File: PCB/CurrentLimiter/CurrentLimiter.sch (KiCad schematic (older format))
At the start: 22 parts, among them P1 CONN_01X06, Q1 Q_PMOS_DGS, Q2 2N2222, Q3 2N2222, Q4 2N2222, U1 LM358

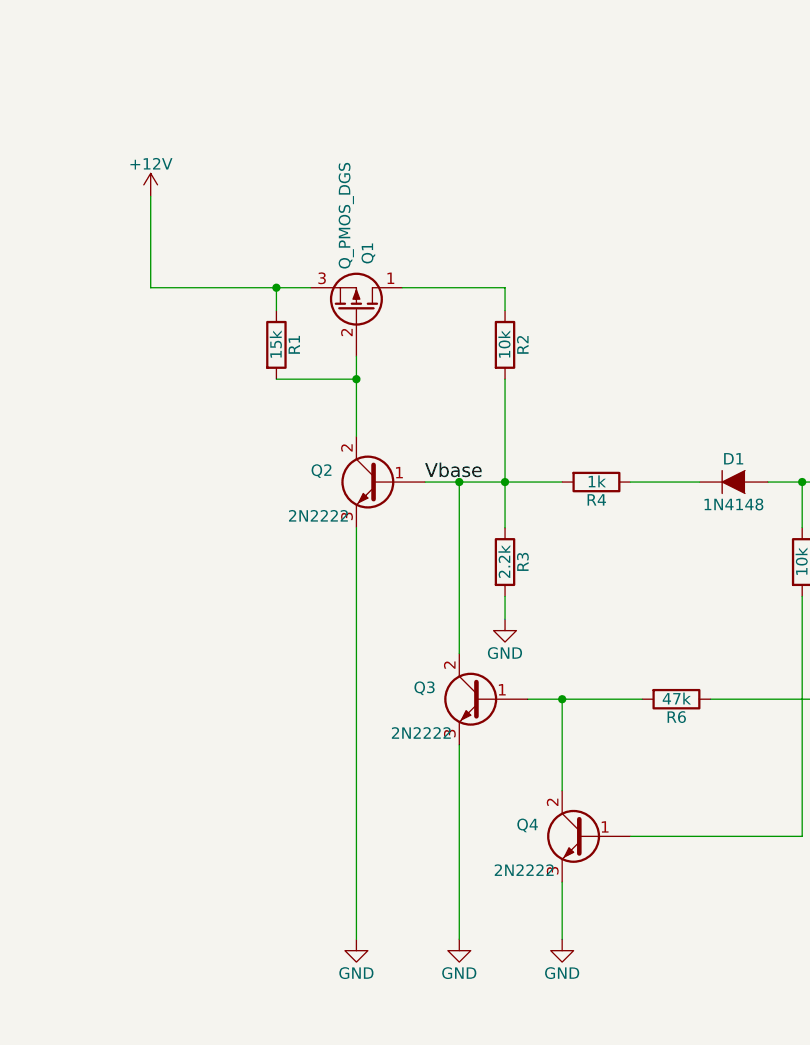
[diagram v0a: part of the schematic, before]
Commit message: Footprints for transistors added
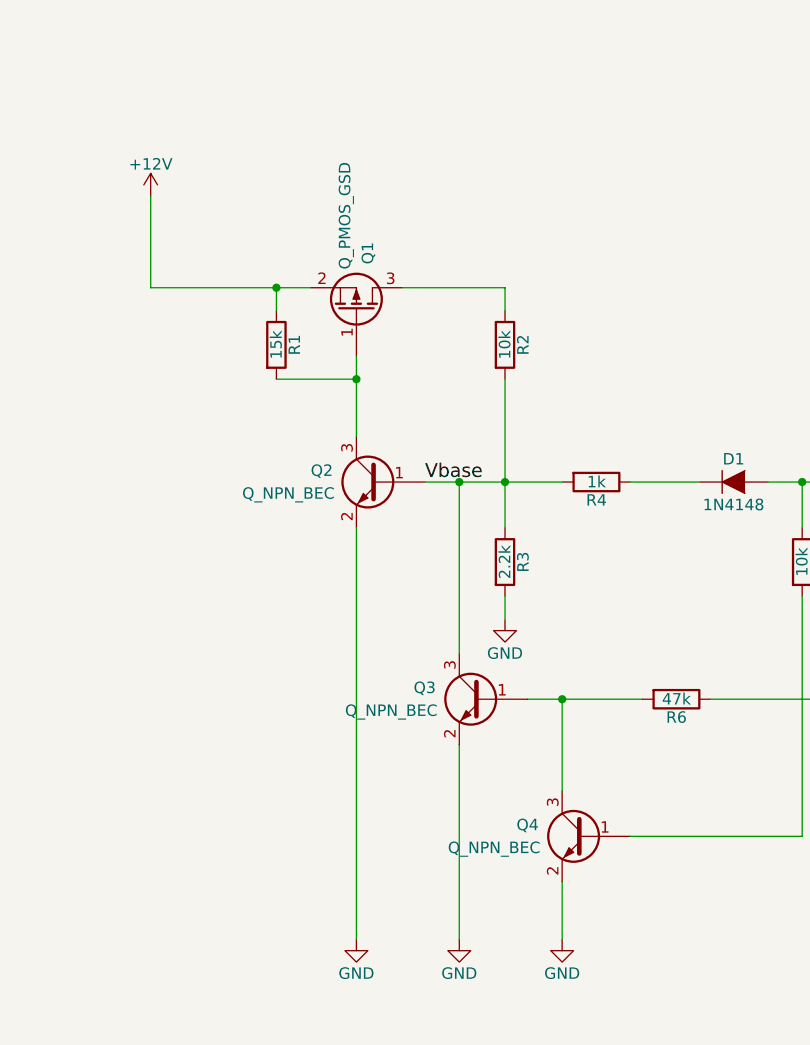
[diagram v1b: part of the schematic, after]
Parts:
- removed Q1: Q_PMOS_DGS, symbol Q_PMOS_DGS
- removed Q2, Q3, Q4: 2N2222, TO_SOT_Packages_SMD:SOT-23_Handsoldering, symbol Q_NPN_BCE
- added Q1: Q_PMOS_GSD, TO_SOT_Packages_SMD:SOT-23_Handsoldering, symbol Q_PMOS_GSD
- added Q2, Q3, Q4: Q_NPN_BEC, TO_SOT_Packages_SMD:SOT-23_Handsoldering, symbol Q_NPN_BEC
- D1: footprint (none) -> Diodes_SMD:D_SOD-123
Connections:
- net +12V: now also Q1.2 (S)
- net GND: now also Q2.2 (E), Q3.2 (E), Q4.2 (E)
- net Vbase: now also Q2.1 (B), Q3.3 (C)
- net at R2.1: now also Q1.3 (D)
- net at R1.2: now also Q1.1 (G), Q2.3 (C)
- net at R6.2: now also Q3.1 (B), Q4.3 (C)
- net at R5.2: now also Q4.1 (B)
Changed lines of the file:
@@
 LIBS:contrib
 LIBS:valves
+LIBS:CurrentLimiter-cache
 EELAYER 25 0
 EELAYER END
@@
 $EndDescr
 $Comp
-L Q_PMOS_DGS Q1
-U 1 1 58E136A7
-P 3450 2550
-F 0 "Q1" H 3750 2600 50  0000 R CNN
-F 1 "Q_PMOS_DGS" H 4100 2500 50  0000 R CNN
-F 2 "" H 3650 2650 50  0001 C CNN
-F 3 "" H 3450 2550 50  0000 C CNN
-	1    3450 2550
-	0    1    -1   0
-$EndComp
-$Comp
-L Q_NPN_BCE Q2
-U 1 1 58E1386B
-P 3550 3300
-F 0 "Q2" H 3850 3350 50  0000 R CNN
-F 1 "2N2222" H 3950 3150 50  0000 R CNN
-F 2 "TO_SOT_Packages_SMD:SOT-23_Handsoldering" H 3750 3400 50  0001 C CNN
-F 3 "" H 3550 3300 50  0000 C CNN
-	1    3550 3300
-	-1   0    0    -1
-$EndComp
-$Comp
 L R R1
 U 1 1 58E138AA
@@
 Connection ~ 3450 2850
 $Comp
-L Q_NPN_BCE Q3
-U 1 1 58E13A50
-P 4000 4250
-F 0 "Q3" H 4300 4300 50  0000 R CNN
-F 1 "2N2222" H 4400 4100 50  0000 R CNN
-F 2 "TO_SOT_Packages_SMD:SOT-23_Handsoldering" H 4200 4350 50  0001 C CNN
-F 3 "" H 4000 4250 50  0000 C CNN
-	1    4000 4250
-	-1   0    0    -1
-$EndComp
-$Comp
-L Q_NPN_BCE Q4
-U 1 1 58E13A9F
-P 4450 4850
-F 0 "Q4" H 4750 4900 50  0000 R CNN
-F 1 "2N2222" H 4850 4700 50  0000 R CNN
-F 2 "TO_SOT_Packages_SMD:SOT-23_Handsoldering" H 4650 4950 50  0001 C CNN
-F 3 "" H 4450 4850 50  0000 C CNN
-	1    4450 4850
-	-1   0    0    -1
-$EndComp
-$Comp
 L R R2
 U 1 1 58E13BAC
@@
 F 0 "D1" H 5100 3400 50  0000 C CNN
 F 1 "1N4148" H 5100 3200 50  0000 C CNN
-F 2 "" H 5100 3300 50  0001 C CNN
+F 2 "Diodes_SMD:D_SOD-123" H 5100 3300 50  0001 C CNN
 F 3 "" H 5100 3300 50  0000 C CNN
 	1    5100 3300
@@
 Connection ~ 3100 2450
 $Comp
-L GND #PWR01
+L GND #PWR5
 U 1 1 58E14C1E
 P 4350 5300
-F 0 "#PWR01" H 4350 5050 50  0001 C CNN
+F 0 "#PWR5" H 4350 5050 50  0001 C CNN
 F 1 "GND" H 4350 5150 50  0000 C CNN
 F 2 "" H 4350 5300 50  0000 C CNN
@@
 $EndComp
 $Comp
-L GND #PWR02
+L GND #PWR3
 U 1 1 58E14C51
 P 3900 5300
-F 0 "#PWR02" H 3900 5050 50  0001 C CNN
+F 0 "#PWR3" H 3900 5050 50  0001 C CNN
 F 1 "GND" H 3900 5150 50  0000 C CNN
 F 2 "" H 3900 5300 50  0000 C CNN
@@
 	3900 5300 3900 4450
 $Comp
-L GND #PWR03
+L GND #PWR2
 U 1 1 58E14DA9
 P 3450 5300
-F 0 "#PWR03" H 3450 5050 50  0001 C CNN
+F 0 "#PWR2" H 3450 5050 50  0001 C CNN
 F 1 "GND" H 3450 5150 50  0000 C CNN
 F 2 "" H 3450 5300 50  0000 C CNN
@@
 	3450 5300 3450 3500
 $Comp
-L GND #PWR04
+L GND #PWR4
 U 1 1 58E14FAF
 P 4100 3900
-F 0 "#PWR04" H 4100 3650 50  0001 C CNN
+F 0 "#PWR4" H 4100 3650 50  0001 C CNN
 F 1 "GND" H 4100 3750 50  0000 C CNN
 F 2 "" H 4100 3900 50  0000 C CNN
@@
 	5000 4250 6050 4250
 $Comp
-L GND #PWR05
+L GND #PWR7
 U 1 1 58E15CDD
 P 6450 5300
-F 0 "#PWR05" H 6450 5050 50  0001 C CNN
+F 0 "#PWR7" H 6450 5050 50  0001 C CNN
 F 1 "GND" H 6450 5150 50  0000 C CNN
 F 2 "" H 6450 5300 50  0000 C CNN
@@
 Connection ~ 8400 4450
 $Comp
-L GND #PWR06
+L GND #PWR10
 U 1 1 58E17521
 P 8400 5300
-F 0 "#PWR06" H 8400 5050 50  0001 C CNN
+F 0 "#PWR10" H 8400 5050 50  0001 C CNN
 F 1 "GND" H 8400 5150 50  0000 C CNN
 F 2 "" H 8400 5300 50  0000 C CNN
@@
 	8400 5300 8400 5000
 $Comp
-L GND #PWR07
+L GND #PWR9
 U 1 1 58E17943
 P 8050 5300
-F 0 "#PWR07" H 8050 5050 50  0001 C CNN
+F 0 "#PWR9" H 8050 5050 50  0001 C CNN
 F 1 "GND" H 8050 5150 50  0000 C CNN
 F 2 "" H 8050 5300 50  0000 C CNN
@@
 	6850 4150 6850 3300
 $Comp
-L +12V #PWR08
+L +12V #PWR1
 U 1 1 58E198F4
 P 2550 2050
-F 0 "#PWR08" H 2550 1900 50  0001 C CNN
+F 0 "#PWR1" H 2550 1900 50  0001 C CNN
 F 1 "+12V" H 2550 2190 50  0000 C CNN
 F 2 "" H 2550 2050 50  0000 C CNN
@@
 	2550 2450 2550 2050
 $Comp
-L +12V #PWR09
+L +12V #PWR6
 U 1 1 58E1998A
 P 6450 3650
-F 0 "#PWR09" H 6450 3500 50  0001 C CNN
+F 0 "#PWR6" H 6450 3500 50  0001 C CNN
 F 1 "+12V" H 6450 3790 50  0000 C CNN
 F 2 "" H 6450 3650 50  0000 C CNN
@@
 	6450 3950 6450 3650
 $Comp
-L +12V #PWR010
+L +12V #PWR8
 U 1 1 58E19BCF
 P 8050 3650
-F 0 "#PWR010" H 8050 3500 50  0001 C CNN
+F 0 "#PWR8" H 8050 3500 50  0001 C CNN
 F 1 "+12V" H 8050 3790 50  0000 C CNN
 F 2 "" H 8050 3650 50  0000 C CNN
@@
 $EndComp
 $Comp
-L +12V #PWR011
+L +12V #PWR11
 U 1 1 58E1E64F
 P 8950 900
-F 0 "#PWR011" H 8950 750 50  0001 C CNN
+F 0 "#PWR11" H 8950 750 50  0001 C CNN
 F 1 "+12V" H 8950 1040 50  0000 C CNN
 F 2 "" H 8950 900 50  0000 C CNN
@@
 $EndComp
 $Comp
-L GND #PWR012
+L GND #PWR12
 U 1 1 58E1E812
 P 9000 1800
-F 0 "#PWR012" H 9000 1550 50  0001 C CNN
+F 0 "#PWR12" H 9000 1550 50  0001 C CNN
 F 1 "GND" H 9000 1650 50  0000 C CNN
 F 2 "" H 9000 1800 50  0000 C CNN
@@
 Wire Wire Line
 	2550 2450 3250 2450
+$Comp
+L Q_NPN_BEC Q2
+U 1 1 58E4ED74
+P 3550 3300
+F 0 "Q2" H 3850 3350 50  0000 R CNN
+F 1 "Q_NPN_BEC" H 4150 3250 50  0000 R CNN
+F 2 "TO_SOT_Packages_SMD:SOT-23_Handsoldering" H 3750 3400 50  0001 C CNN
+F 3 "http://lv.farnell.com/nxp/bcx70h/transistor-npn-sot-23/dp/1081282" H 3550 3300 50  0001 C CNN
+F 4 "http://lv.farnell.com/fairchild-semiconductor/bcw66g/transistor-npn-smd-sot-23/dp/1467891" H 3550 3300 60  0001 C CNN "Alternate part"
+	1    3550 3300
+	-1   0    0    -1
+$EndComp
+$Comp
+L Q_NPN_BEC Q3
+U 1 1 58E4F17E
+P 4000 4250
+F 0 "Q3" H 4300 4300 50  0000 R CNN
+F 1 "Q_NPN_BEC" H 4600 4200 50  0000 R CNN
+F 2 "TO_SOT_Packages_SMD:SOT-23_Handsoldering" H 4200 4350 50  0001 C CNN
+F 3 "http://lv.farnell.com/nxp/bcx70h/transistor-npn-sot-23/dp/1081282" H 4000 4250 50  0001 C CNN
+F 4 "http://lv.farnell.com/fairchild-semiconductor/bcw66g/transistor-npn-smd-sot-23/dp/1467891" H 4000 4250 60  0001 C CNN "Alternate part"
+	1    4000 4250
+	-1   0    0    -1
+$EndComp
+$Comp
+L Q_NPN_BEC Q4
+U 1 1 58E4F224
+P 4450 4850
+F 0 "Q4" H 4750 4900 50  0000 R CNN
+F 1 "Q_NPN_BEC" H 5050 4800 50  0000 R CNN
+F 2 "TO_SOT_Packages_SMD:SOT-23_Handsoldering" H 4650 4950 50  0001 C CNN
+F 3 "http://lv.farnell.com/nxp/bcx70h/transistor-npn-sot-23/dp/1081282" H 4450 4850 50  0001 C CNN
+F 4 "http://lv.farnell.com/fairchild-semiconductor/bcw66g/transistor-npn-smd-sot-23/dp/1467891" H 4450 4850 60  0001 C CNN "Alternate part"
+	1    4450 4850
+	-1   0    0    -1
+$EndComp
+$Comp
+L Q_PMOS_GSD Q1
+U 1 1 58E4F551
+P 3450 2550
+F 0 "Q1" H 3750 2600 50  0000 R CNN
+F 1 "Q_PMOS_GSD" H 4100 2500 50  0000 R CNN
+F 2 "TO_SOT_Packages_SMD:SOT-23_Handsoldering" H 3650 2650 50  0001 C CNN
+F 3 "http://lv.farnell.com/infineon/irlml9301trpbf/mosfet-diode-p-ch-30v-3-6a-sot23/dp/1831089" H 3450 2550 50  0001 C CNN
+	1    3450 2550
+	0    1    -1   0
+$EndComp
 $EndSCHEMATC

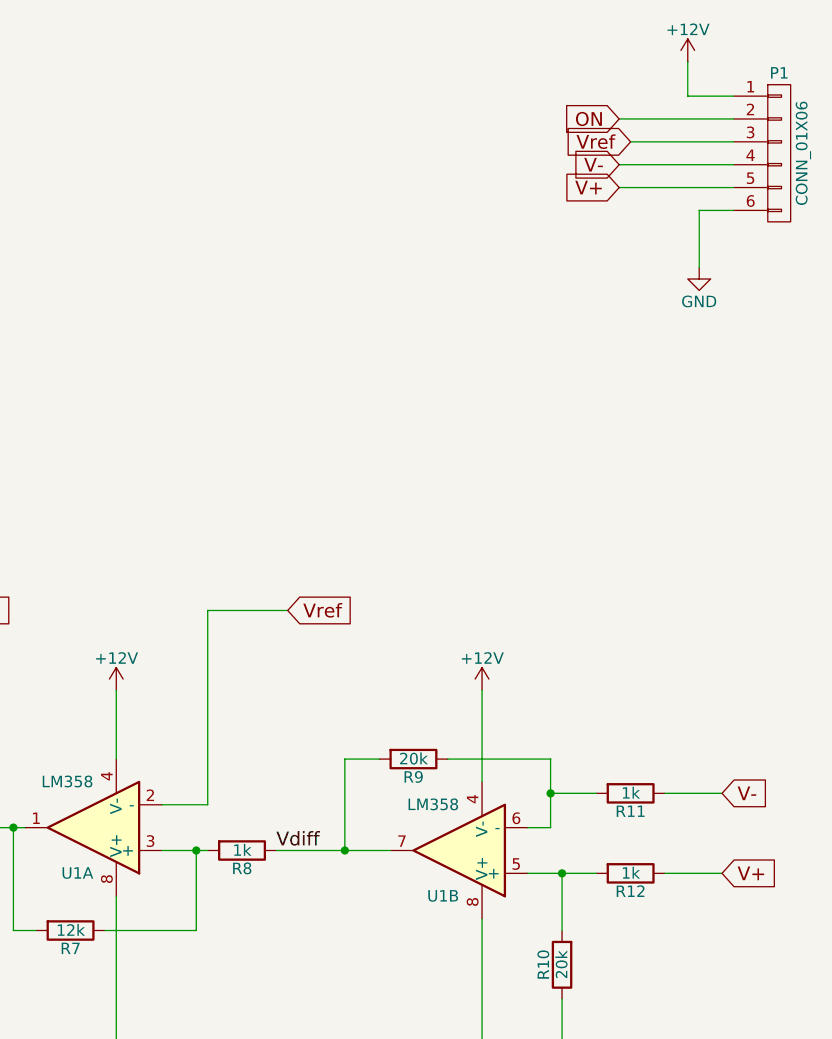
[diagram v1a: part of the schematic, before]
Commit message: Added header connectors for OpAmp modules
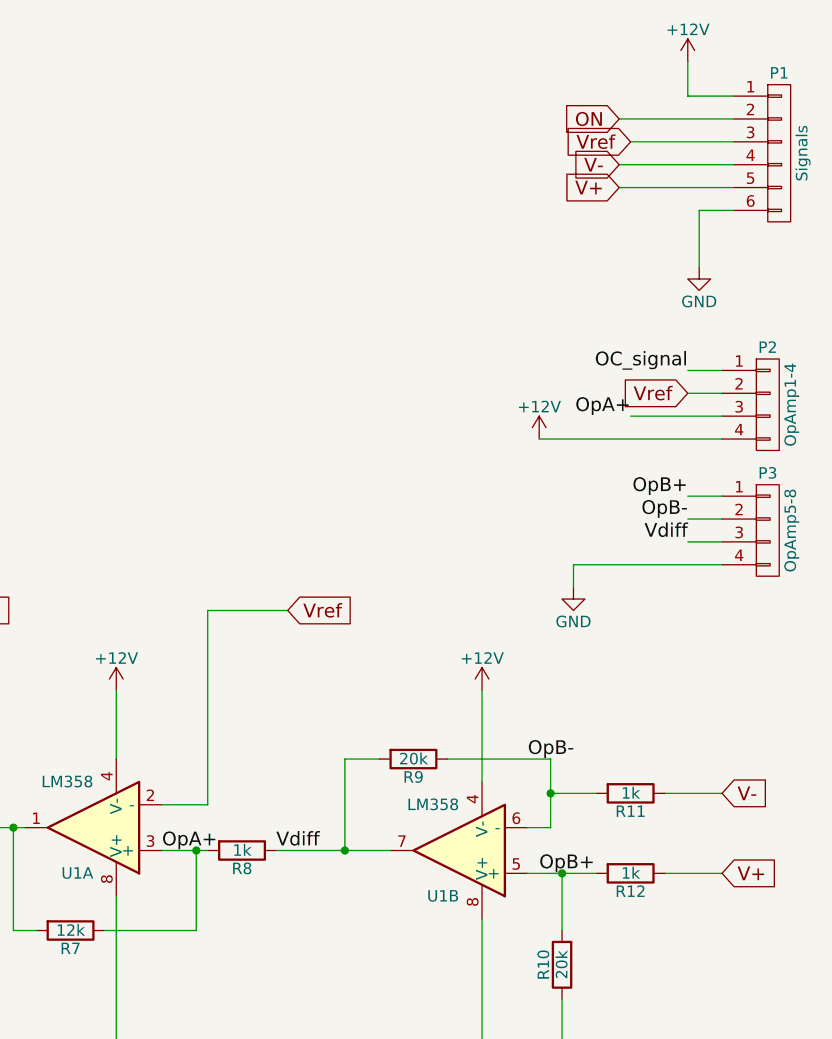
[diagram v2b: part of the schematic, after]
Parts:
- added P2: OpAmp1-4, symbol CONN_01X04
- added P3: OpAmp5-8, symbol CONN_01X04
- P1: value CONN_01X06 -> Signals
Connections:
- net +12V: now also P2.4 (P4)
- net GND: now also P3.4 (P4)
- net OC_signal: now also P2.1 (P1)
- net Vdiff: now also P3.3 (P3)
- net Vref: now also P2.2 (P2)
- net OpA+: now reaches R7.1, R8.2, U1.3 (+)
- net OpA+: now also P2.3 (P3)
- net OpB+: now reaches R10.2, R12.2, U1.5 (+)
- net OpB+: now also P3.1 (P1)
- net OpB-: now reaches R11.2, R9.1, U1.6 (-)
- net OpB-: now also P3.2 (P2)
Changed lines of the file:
@@
 Connection ~ 8400 4450
 $Comp
-L GND #PWR10
+L GND #PWR11
 U 1 1 58E17521
 P 8400 5300
-F 0 "#PWR10" H 8400 5050 50  0001 C CNN
+F 0 "#PWR11" H 8400 5050 50  0001 C CNN
 F 1 "GND" H 8400 5150 50  0000 C CNN
 F 2 "" H 8400 5300 50  0000 C CNN
@@
 P 9350 1300
 F 0 "P1" H 9350 1650 50  0000 C CNN
-F 1 "CONN_01X06" V 9450 1300 50  0000 C CNN
+F 1 "Signals" V 9450 1300 50  0000 C CNN
 F 2 "Pin_Headers:Pin_Header_Straight_1x06_Pitch2.54mm" H 9350 1300 50  0001 C CNN
 F 3 "" H 9350 1300 50  0000 C CNN
@@
 $EndComp
 $Comp
-L +12V #PWR11
+L +12V #PWR13
 U 1 1 58E1E64F
 P 8950 900
-F 0 "#PWR11" H 8950 750 50  0001 C CNN
+F 0 "#PWR13" H 8950 750 50  0001 C CNN
 F 1 "+12V" H 8950 1040 50  0000 C CNN
 F 2 "" H 8950 900 50  0000 C CNN
@@
 $EndComp
 $Comp
-L GND #PWR12
+L GND #PWR14
 U 1 1 58E1E812
 P 9000 1800
-F 0 "#PWR12" H 9000 1550 50  0001 C CNN
+F 0 "#PWR14" H 9000 1550 50  0001 C CNN
 F 1 "GND" H 9000 1650 50  0000 C CNN
 F 2 "" H 9000 1800 50  0000 C CNN
@@
 	0    1    -1   0
 $EndComp
+$Comp
+L CONN_01X04 P2
+U 1 1 58E5112F
+P 9300 2400
+F 0 "P2" H 9300 2650 50  0000 C CNN
+F 1 "OpAmp1-4" V 9400 2400 50  0000 C CNN
+F 2 "" H 9300 2400 50  0000 C CNN
+F 3 "" H 9300 2400 50  0000 C CNN
+	1    9300 2400
+	1    0    0    -1
+$EndComp
+$Comp
+L CONN_01X04 P3
+U 1 1 58E51184
+P 9300 2950
+F 0 "P3" H 9300 3200 50  0000 C CNN
+F 1 "OpAmp5-8" V 9400 2950 50  0000 C CNN
+F 2 "" H 9300 2950 50  0000 C CNN
+F 3 "" H 9300 2950 50  0000 C CNN
+	1    9300 2950
+	1    0    0    -1
+$EndComp
+Wire Wire Line
+	8950 2250 9100 2250
+Wire Wire Line
+	8950 2350 9100 2350
+Wire Wire Line
+	8700 2450 9100 2450
+Wire Wire Line
+	8300 2550 9100 2550
+Wire Wire Line
+	8950 2800 9100 2800
+Wire Wire Line
+	8950 2900 9100 2900
+Wire Wire Line
+	8950 3000 9100 3000
+Wire Wire Line
+	8450 3100 9100 3100
+Text Label 8950 2250 2    60   ~ 0
+OC_signal
+Text GLabel 8950 2350 0    60   Input ~ 0
+Vref
+Text Label 6650 4350 0    60   ~ 0
+OpA+
+Text Label 8700 2450 2    60   ~ 0
+OpA+
+$Comp
+L +12V #PWR10
+U 1 1 58E52D29
+P 8300 2550
+F 0 "#PWR10" H 8300 2400 50  0001 C CNN
+F 1 "+12V" H 8300 2690 50  0000 C CNN
+F 2 "" H 8300 2550 50  0000 C CNN
+F 3 "" H 8300 2550 50  0000 C CNN
+	1    8300 2550
+	1    0    0    -1
+$EndComp
+Text Label 8300 4450 0    60   ~ 0
+OpB+
+Text Label 8950 2800 2    60   ~ 0
+OpB+
+Text Label 8250 3950 0    60   ~ 0
+OpB-
+Text Label 8950 2900 2    60   ~ 0
+OpB-
+Text Label 8950 3000 2    60   ~ 0
+Vdiff
+$Comp
+L GND #PWR12
+U 1 1 58E52FB1
+P 8450 3200
+F 0 "#PWR12" H 8450 2950 50  0001 C CNN
+F 1 "GND" H 8450 3050 50  0000 C CNN
+F 2 "" H 8450 3200 50  0000 C CNN
+F 3 "" H 8450 3200 50  0000 C CNN
+	1    8450 3200
+	1    0    0    -1
+$EndComp
+Wire Wire Line
+	8450 3200 8450 3100
 $EndSCHEMATC

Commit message: Initial over-current PCB layout file
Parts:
- P2, P3: footprint (none) -> Pin_Headers:Pin_Header_Straight_1x04_Pitch2.54mm
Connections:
- net GND: now also P3.1 (P1); no longer P3.4 (P4)
- net OpB+: now also P3.4 (P4); no longer P3.1 (P1)
- net OpB-: now also P3.3 (P3); no longer P3.2 (P2)
- net Vdiff: now also P3.2 (P2); no longer P3.3 (P3)
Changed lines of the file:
@@
 Connection ~ 3100 2450
 $Comp
-L GND #PWR5
+L GND #PWR01
 U 1 1 58E14C1E
 P 4350 5300
-F 0 "#PWR5" H 4350 5050 50  0001 C CNN
+F 0 "#PWR01" H 4350 5050 50  0001 C CNN
 F 1 "GND" H 4350 5150 50  0000 C CNN
 F 2 "" H 4350 5300 50  0000 C CNN
@@
 $EndComp
 $Comp
-L GND #PWR3
+L GND #PWR02
 U 1 1 58E14C51
 P 3900 5300
-F 0 "#PWR3" H 3900 5050 50  0001 C CNN
+F 0 "#PWR02" H 3900 5050 50  0001 C CNN
 F 1 "GND" H 3900 5150 50  0000 C CNN
 F 2 "" H 3900 5300 50  0000 C CNN
@@
 	3900 5300 3900 4450
 $Comp
-L GND #PWR2
+L GND #PWR03
 U 1 1 58E14DA9
 P 3450 5300
-F 0 "#PWR2" H 3450 5050 50  0001 C CNN
+F 0 "#PWR03" H 3450 5050 50  0001 C CNN
 F 1 "GND" H 3450 5150 50  0000 C CNN
 F 2 "" H 3450 5300 50  0000 C CNN
@@
 	3450 5300 3450 3500
 $Comp
-L GND #PWR4
+L GND #PWR04
 U 1 1 58E14FAF
 P 4100 3900
-F 0 "#PWR4" H 4100 3650 50  0001 C CNN
+F 0 "#PWR04" H 4100 3650 50  0001 C CNN
 F 1 "GND" H 4100 3750 50  0000 C CNN
 F 2 "" H 4100 3900 50  0000 C CNN
@@
 	5000 4250 6050 4250
 $Comp
-L GND #PWR7
+L GND #PWR05
 U 1 1 58E15CDD
 P 6450 5300
-F 0 "#PWR7" H 6450 5050 50  0001 C CNN
+F 0 "#PWR05" H 6450 5050 50  0001 C CNN
 F 1 "GND" H 6450 5150 50  0000 C CNN
 F 2 "" H 6450 5300 50  0000 C CNN
@@
 Connection ~ 8400 4450
 $Comp
-L GND #PWR11
+L GND #PWR06
 U 1 1 58E17521
 P 8400 5300
-F 0 "#PWR11" H 8400 5050 50  0001 C CNN
+F 0 "#PWR06" H 8400 5050 50  0001 C CNN
 F 1 "GND" H 8400 5150 50  0000 C CNN
 F 2 "" H 8400 5300 50  0000 C CNN
@@
 	8400 5300 8400 5000
 $Comp
-L GND #PWR9
+L GND #PWR07
 U 1 1 58E17943
 P 8050 5300
-F 0 "#PWR9" H 8050 5050 50  0001 C CNN
+F 0 "#PWR07" H 8050 5050 50  0001 C CNN
 F 1 "GND" H 8050 5150 50  0000 C CNN
 F 2 "" H 8050 5300 50  0000 C CNN
@@
 	6850 4150 6850 3300
 $Comp
-L +12V #PWR1
+L +12V #PWR08
 U 1 1 58E198F4
 P 2550 2050
-F 0 "#PWR1" H 2550 1900 50  0001 C CNN
+F 0 "#PWR08" H 2550 1900 50  0001 C CNN
 F 1 "+12V" H 2550 2190 50  0000 C CNN
 F 2 "" H 2550 2050 50  0000 C CNN
@@
 	2550 2450 2550 2050
 $Comp
-L +12V #PWR6
+L +12V #PWR09
 U 1 1 58E1998A
 P 6450 3650
-F 0 "#PWR6" H 6450 3500 50  0001 C CNN
+F 0 "#PWR09" H 6450 3500 50  0001 C CNN
 F 1 "+12V" H 6450 3790 50  0000 C CNN
 F 2 "" H 6450 3650 50  0000 C CNN
@@
 	6450 3950 6450 3650
 $Comp
-L +12V #PWR8
+L +12V #PWR010
 U 1 1 58E19BCF
 P 8050 3650
-F 0 "#PWR8" H 8050 3500 50  0001 C CNN
+F 0 "#PWR010" H 8050 3500 50  0001 C CNN
 F 1 "+12V" H 8050 3790 50  0000 C CNN
 F 2 "" H 8050 3650 50  0000 C CNN
@@
 $EndComp
 $Comp
-L +12V #PWR13
+L +12V #PWR011
 U 1 1 58E1E64F
 P 8950 900
-F 0 "#PWR13" H 8950 750 50  0001 C CNN
+F 0 "#PWR011" H 8950 750 50  0001 C CNN
 F 1 "+12V" H 8950 1040 50  0000 C CNN
 F 2 "" H 8950 900 50  0000 C CNN
@@
 $EndComp
 $Comp
-L GND #PWR14
+L GND #PWR012
 U 1 1 58E1E812
 P 9000 1800
-F 0 "#PWR14" H 9000 1550 50  0001 C CNN
+F 0 "#PWR012" H 9000 1550 50  0001 C CNN
 F 1 "GND" H 9000 1650 50  0000 C CNN
 F 2 "" H 9000 1800 50  0000 C CNN
@@
 F 0 "P2" H 9300 2650 50  0000 C CNN
 F 1 "OpAmp1-4" V 9400 2400 50  0000 C CNN
-F 2 "" H 9300 2400 50  0000 C CNN
+F 2 "Pin_Headers:Pin_Header_Straight_1x04_Pitch2.54mm" H 9300 2400 50  0001 C CNN
 F 3 "" H 9300 2400 50  0000 C CNN
 	1    9300 2400
@@
 F 0 "P3" H 9300 3200 50  0000 C CNN
 F 1 "OpAmp5-8" V 9400 2950 50  0000 C CNN
-F 2 "" H 9300 2950 50  0000 C CNN
+F 2 "Pin_Headers:Pin_Header_Straight_1x04_Pitch2.54mm" H 9300 2950 50  0001 C CNN
 F 3 "" H 9300 2950 50  0000 C CNN
 	1    9300 2950
@@
 	8300 2550 9100 2550
 Wire Wire Line
-	8950 2800 9100 2800
+	8450 2800 9100 2800
 Wire Wire Line
 	8950 2900 9100 2900
-Wire Wire Line
-	8950 3000 9100 3000
-Wire Wire Line
-	8450 3100 9100 3100
 Text Label 8950 2250 2    60   ~ 0
 OC_signal
@@
 OpA+
 $Comp
-L +12V #PWR10
+L +12V #PWR013
 U 1 1 58E52D29
 P 8300 2550
-F 0 "#PWR10" H 8300 2400 50  0001 C CNN
+F 0 "#PWR013" H 8300 2400 50  0001 C CNN
 F 1 "+12V" H 8300 2690 50  0000 C CNN
 F 2 "" H 8300 2550 50  0000 C CNN
@@
 Text Label 8300 4450 0    60   ~ 0
 OpB+
-Text Label 8950 2800 2    60   ~ 0
+Text Label 8950 3100 2    60   ~ 0
 OpB+
 Text Label 8250 3950 0    60   ~ 0
 OpB-
+Text Label 8950 3000 2    60   ~ 0
+OpB-
 Text Label 8950 2900 2    60   ~ 0
-OpB-
-Text Label 8950 3000 2    60   ~ 0
 Vdiff
 $Comp
-L GND #PWR12
+L GND #PWR014
 U 1 1 58E52FB1
 P 8450 3200
-F 0 "#PWR12" H 8450 2950 50  0001 C CNN
+F 0 "#PWR014" H 8450 2950 50  0001 C CNN
 F 1 "GND" H 8450 3050 50  0000 C CNN
 F 2 "" H 8450 3200 50  0000 C CNN
@@
 $EndComp
 Wire Wire Line
-	8450 3200 8450 3100
+	8450 2800 8450 3200
+Wire Wire Line
+	8950 3000 9100 3000
+Wire Wire Line
+	8950 3100 9100 3100
 $EndSCHEMATC
